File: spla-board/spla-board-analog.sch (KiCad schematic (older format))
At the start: 23 parts, among them J13 J_ANALOG, J14 J_AREF, U4 AD9280ARS, U5 AD9280ARS, U6 AD9280ARS

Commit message: schematic: Partial rework of analog to use LMH6611 + ADC1173.
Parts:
- removed C16, C18, C19, C20, C22, C23, C24, C26, C27: 0.1uF, Capacitor_SMD:C_0603_1608Metric, symbol Device:C_Small
- removed C17, C21, C25: 10uF, Capacitor_SMD:C_0603_1608Metric, symbol Device:C_Small
- removed U4, U5, U6: AD9280ARS, Package_SO:SSOP-28_5.3x10.2mm_P0.65mm, symbol Analog_ADC:AD9280ARS
- added C?: 0.1uF, Capacitor_SMD:C_0603_1608Metric, symbol Device:C_Small
- added C?: 10uF, Capacitor_SMD:C_0603_1608Metric, symbol Device:C_Small
- added C? (x5): 0.1uF, symbol Device:C_Small
- added C? (x3): 10uF, symbol Device:C_Small
- added C?: 150pF, symbol Device:C_Small
- added C?: 5.6uF, symbol Device:C_Small
- added C?: 390pF, symbol Device:C_Small
- added C?: 0.01uF, symbol Device:C_Small
- added C?: 1nF, symbol Device:C_Small
- added C?: 1uF, symbol Device:C_Small
- added R?: 100,1%, Resistor_SMD:R_0603_1608Metric, symbol Device:R_Small
- added R?: 300, symbol Device:R
- added R?: 720, symbol Device:R
- added R?: 1k, symbol Device:R
- added R? (x2): 14.3k, symbol Device:R_Small
- added R?: 1.24k, symbol Device:R_Small
- added R? (x2): 549, symbol Device:R_Small
- added R?: 22, symbol Device:R_Small
- added U4, U5, U6: ADC1173, symbol Analog_ADC:ADC1173
- added U?: LMH6611, Package_TO_SOT_SMD:TSOT-23-6, symbol Amplifier_Operational:LMH6611
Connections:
- net labels added: ANALOG_AMP_R, ANALOG_SCALED_R, AREF_HI, AREF_LO, OPAMP_2V5
- net labels removed: ANALOG_B_OTR, ANALOG_G_OTR, ANALOG_REF_HI, ANALOG_REF_LO, ANALOG_R_OTR
- wire segments 132 -> 144
- no-connect marks 6 -> 2
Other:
- note added: "AREF_HI = 3.1V"
- note added: "AREF_LO = 1.1V"
- note added: "Ref: ADC1173 Datasheet page 19"
- note added: "Ref: LMH6611 Datasheet Page 25"
- note added: "Ref: Nothing; bogus level divider nonsense"
- note added: "TODO: Correct these values."
- note added: "TODO: Inject opamps to maintain levels"
- note added: "TODO: Recalculate these resistors"
- note added: "TODO: Validate all this nonense with somebody who knows what they're doing."
- note added: "Vrange = 0v - 2.7v"
- note added: "Vrange = 1.2v - 3.0v"
- note removed: "2.702V Reference"
- note removed: "Clamp: Disabled"
- note removed: "Mode: External Reference"
- note removed: "No Standby"
- note removed: "No Tristate"
- note removed: "TODO: Make this voltage reference more easily tweakable."
- moved on the sheet: C14, C15, R15, R16

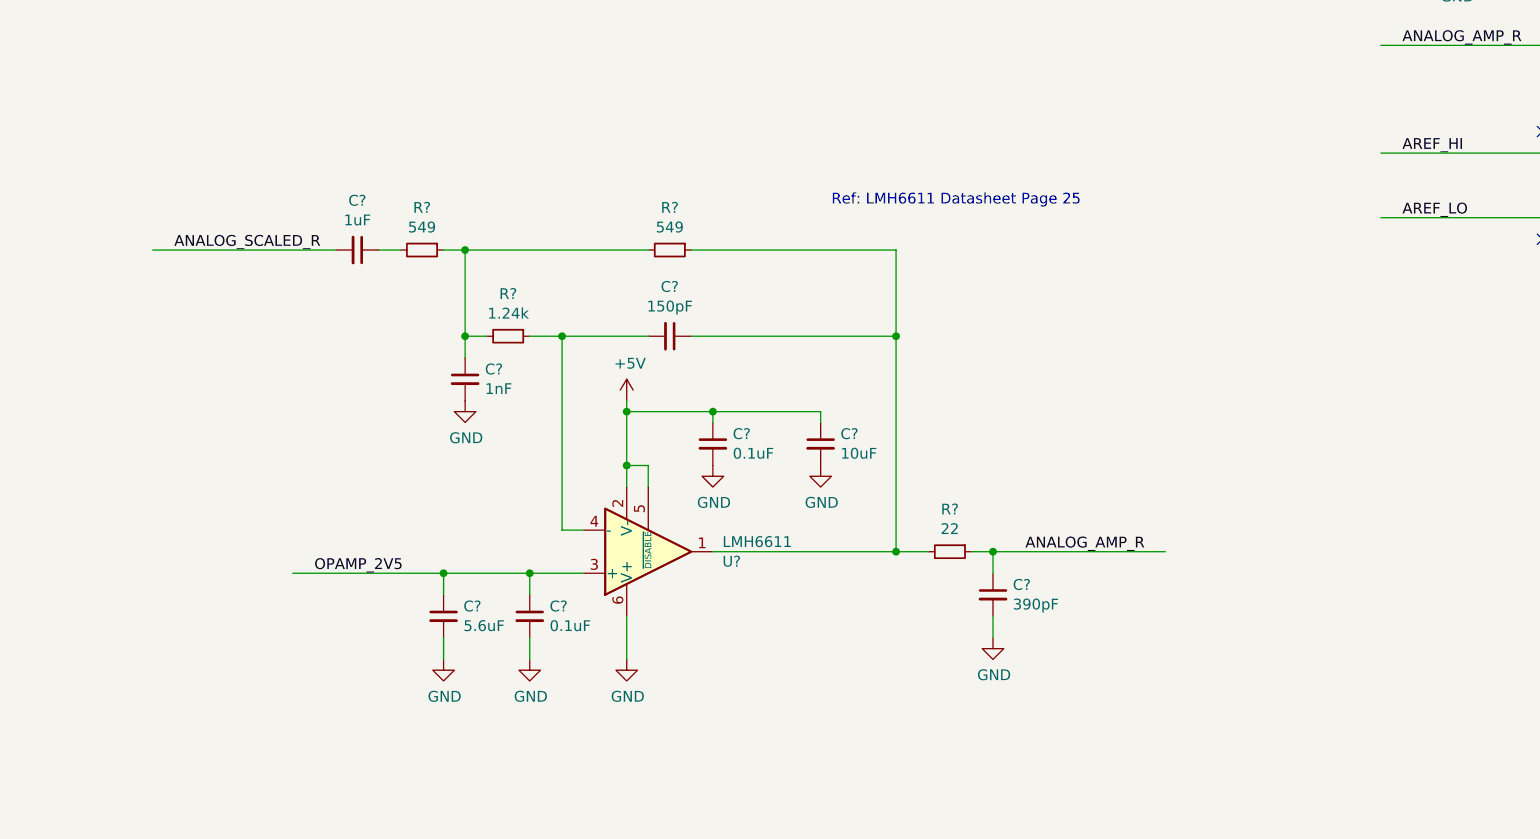
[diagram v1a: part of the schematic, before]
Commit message: schematic: More fiddling with analog.
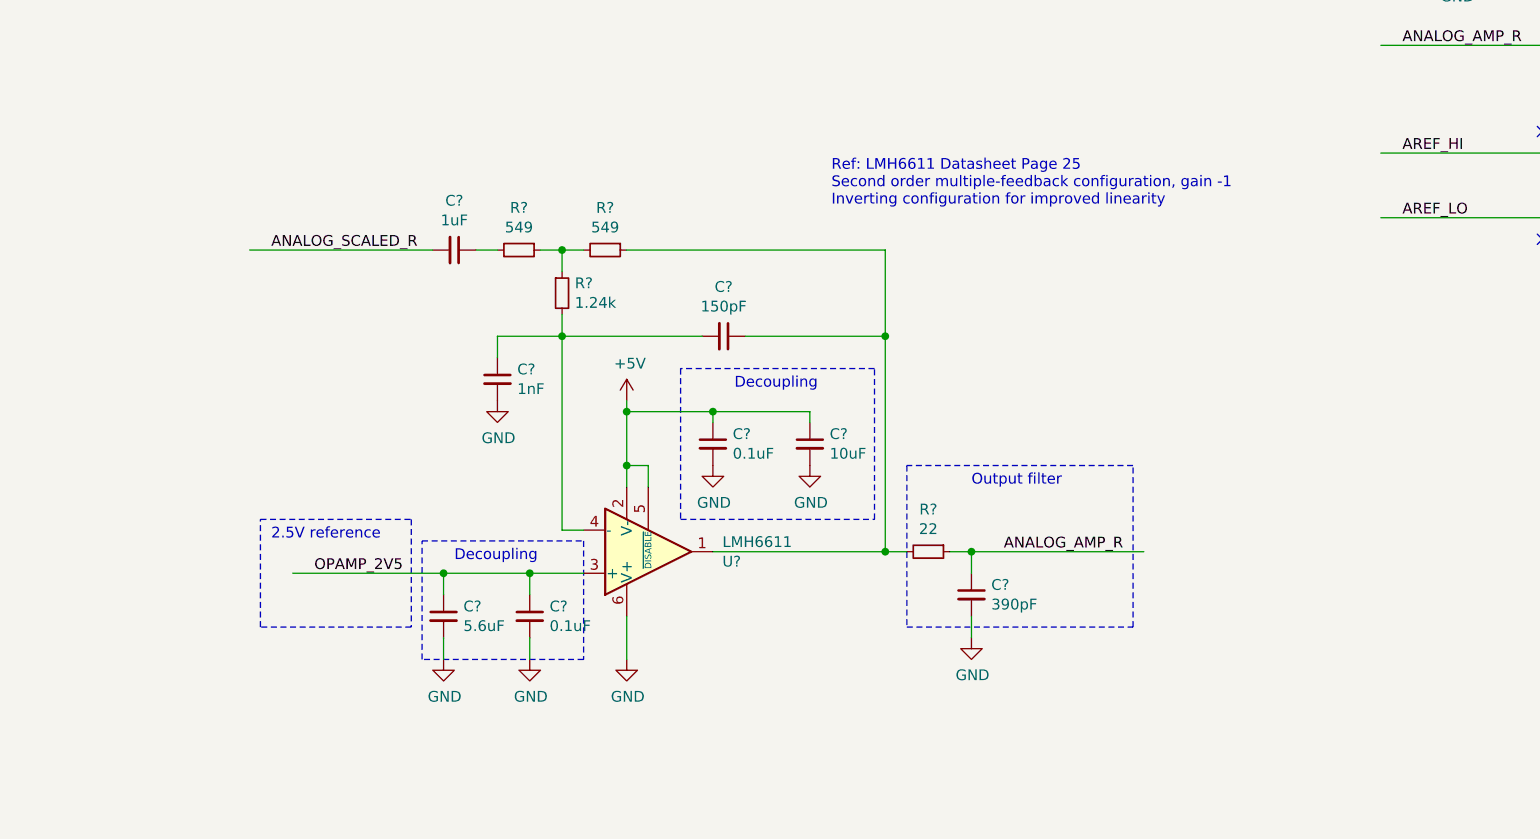
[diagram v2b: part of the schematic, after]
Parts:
- removed R?: 1.24k, symbol Device:R_Small
- added R?: 1.24k, symbol Device:R_Small
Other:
- note added: "2.5V reference"
- note added: "Decoupling"
- note added: "Output filter"
- note added: "Ref: LMH6611 Datasheet Page 25\nSecond order multiple-feedback configuration, gain -1\nInverting configuration for improved linearity"
- note removed: "Ref: LMH6611 Datasheet Page 25"
- moved on the sheet: C?, R?

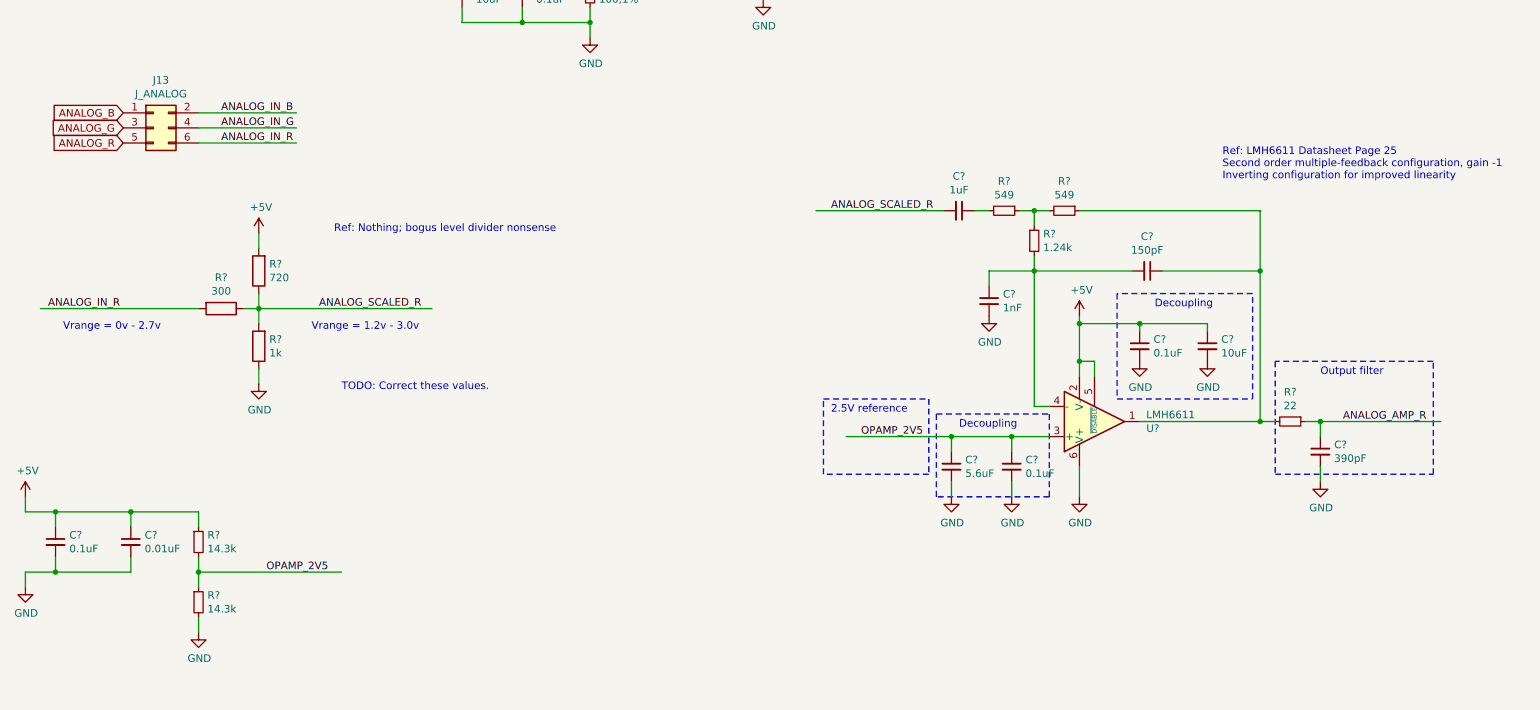
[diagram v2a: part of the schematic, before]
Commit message: schematic: More opamp fiddling.
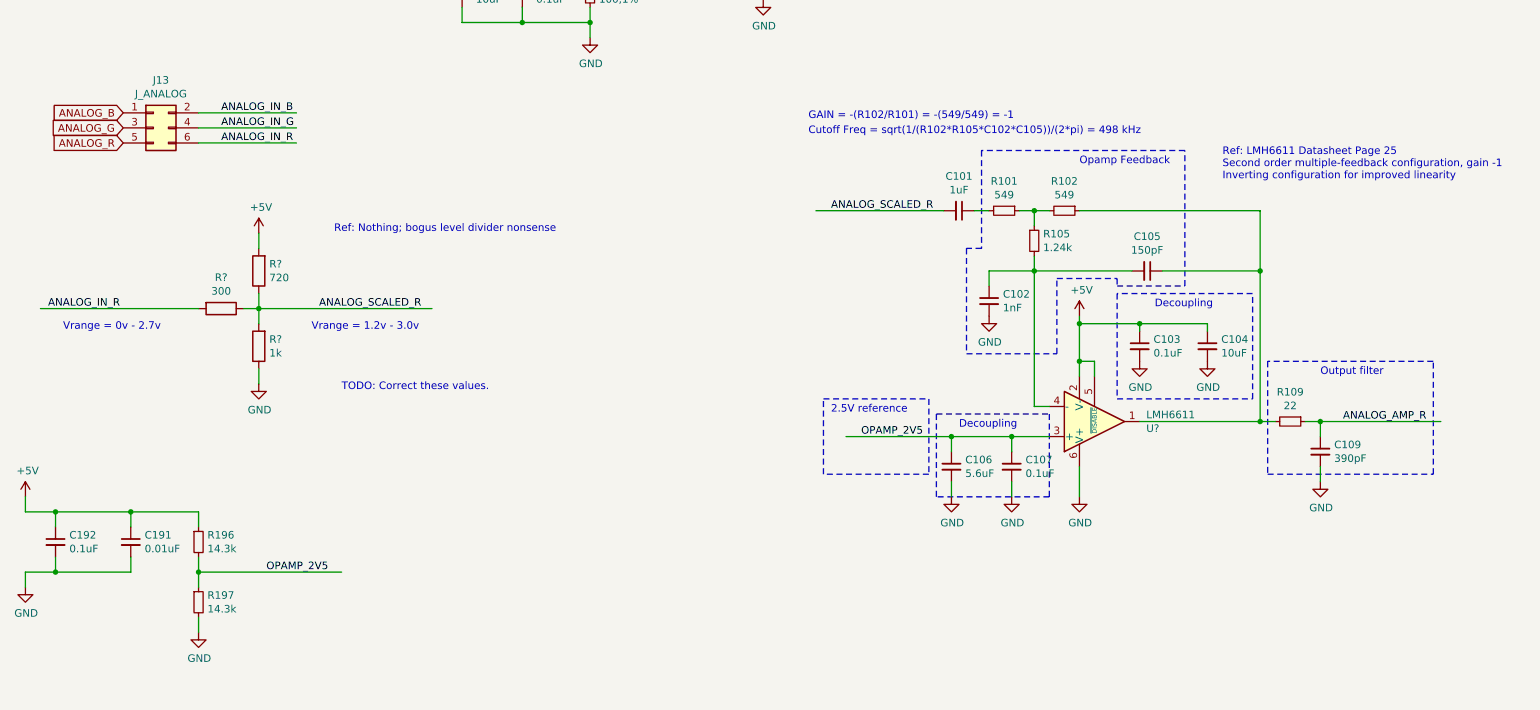
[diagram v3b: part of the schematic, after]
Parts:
- gave numbers to parts that had none: 16
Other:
- note added: "Cutoff Freq = sqrt(1/(R102*R105*C102*C105))/(2*pi) = 498 kHz"
- note added: "GAIN = -(R102/R101) = -(549/549) = -1"
- note added: "Opamp Feedback"
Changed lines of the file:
@@
 	13350 4100 13550 4100
 $Comp
-L power:GND #PWR?
+L power:GND #PWR0196
 U 1 1 5E99F9E8
 P 13550 4200
-F 0 "#PWR?" H 13550 3950 50  0001 C CNN
+F 0 "#PWR0196" H 13550 3950 50  0001 C CNN
 F 1 "GND" H 13555 4027 50  0000 C CNN
 F 2 "" H 13550 4200 50  0001 C CNN
@@
 	12950 4100 12700 4100
 $Comp
-L power:GND #PWR?
+L power:GND #PWR0207
 U 1 1 5E9A0D5B
 P 12700 4200
-F 0 "#PWR?" H 12700 3950 50  0001 C CNN
+F 0 "#PWR0207" H 12700 3950 50  0001 C CNN
 F 1 "GND" H 12705 4027 50  0000 C CNN
 F 2 "" H 12700 4200 50  0001 C CNN
@@
 	13350 2400 13350 2500
 $Comp
-L power:+3V3 #PWR?
+L power:+3V3 #PWR0208
 U 1 1 5E9A44F8
 P 13350 1850
-F 0 "#PWR?" H 13350 1700 50  0001 C CNN
+F 0 "#PWR0208" H 13350 1700 50  0001 C CNN
 F 1 "+3V3" H 13365 2023 50  0000 C CNN
 F 2 "" H 13350 1850 50  0001 C CNN
@@
 	12950 2400 12850 2400
 $Comp
-L power:+5V #PWR?
+L power:+5V #PWR0209
 U 1 1 5E9A757C
 P 12850 1850
-F 0 "#PWR?" H 12850 1700 50  0001 C CNN
+F 0 "#PWR0209" H 12850 1700 50  0001 C CNN
 F 1 "+5V" H 12865 2023 50  0000 C CNN
 F 2 "" H 12850 1850 50  0001 C CNN
@@
 $EndComp
 $Comp
-L power:GND #PWR?
+L power:GND #PWR0210
 U 1 1 5E9A7B1B
 P 8200 5750
-F 0 "#PWR?" H 8200 5500 50  0001 C CNN
+F 0 "#PWR0210" H 8200 5500 50  0001 C CNN
 F 1 "GND" H 8205 5577 50  0000 C CNN
 F 2 "" H 8200 5750 50  0001 C CNN
@@
 $EndComp
 $Comp
-L Device:C_Small C?
+L Device:C_Small C105
 U 1 1 5E9ACDDD
 P 8650 4250
-F 0 "C?" V 8421 4250 50  0000 C CNN
+F 0 "C105" V 8421 4250 50  0000 C CNN
 F 1 "150pF" V 8512 4250 50  0000 C CNN
 F 2 "" H 8650 4250 50  0001 C CNN
@@
 $EndComp
 $Comp
-L Device:C_Small C?
+L Device:C_Small C106
 U 1 1 5E9AE271
 P 7350 5550
-F 0 "C?" H 7442 5596 50  0000 L CNN
+F 0 "C106" H 7442 5596 50  0000 L CNN
 F 1 "5.6uF" H 7442 5505 50  0000 L CNN
 F 2 "" H 7350 5550 50  0001 C CNN
@@
 $EndComp
 $Comp
-L Device:C_Small C?
+L Device:C_Small C107
 U 1 1 5E9AE27B
 P 7750 5550
-F 0 "C?" H 7842 5596 50  0000 L CNN
+F 0 "C107" H 7842 5596 50  0000 L CNN
 F 1 "0.1uF" H 7842 5505 50  0000 L CNN
 F 2 "" H 7750 5550 50  0001 C CNN
@@
 $EndComp
 $Comp
-L Device:C_Small C?
+L Device:C_Small C109
 U 1 1 5E9AFAB1
 P 9800 5450
-F 0 "C?" H 9892 5496 50  0000 L CNN
+F 0 "C109" H 9892 5496 50  0000 L CNN
 F 1 "390pF" H 9892 5405 50  0000 L CNN
 F 2 "" H 9800 5450 50  0001 C CNN
@@
 $EndComp
 $Comp
-L Device:C_Small C?
+L Device:C_Small C192
 U 1 1 5E9B0FA6
 P 1400 6050
-F 0 "C?" H 1492 6096 50  0000 L CNN
+F 0 "C192" H 1492 6096 50  0000 L CNN
 F 1 "0.1uF" H 1492 6005 50  0000 L CNN
 F 2 "" H 1400 6050 50  0001 C CNN
@@
 $EndComp
 $Comp
-L Device:C_Small C?
+L Device:C_Small C191
 U 1 1 5E9B0FB0
 P 1900 6050
-F 0 "C?" H 1992 6096 50  0000 L CNN
+F 0 "C191" H 1992 6096 50  0000 L CNN
 F 1 "0.01uF" H 1992 6005 50  0000 L CNN
 F 2 "" H 1900 6050 50  0001 C CNN
@@
 $EndComp
 $Comp
-L Device:R_Small R?
+L Device:R_Small R197
 U 1 1 5E9B33F1
 P 2350 6450
-F 0 "R?" H 2409 6496 50  0000 L CNN
+F 0 "R197" H 2409 6496 50  0000 L CNN
 F 1 "14.3k" H 2409 6405 50  0000 L CNN
 F 2 "" H 2350 6450 50  0001 C CNN
@@
 $EndComp
 $Comp
-L Device:R_Small R?
+L Device:R_Small R196
 U 1 1 5E9B4953
 P 2350 6050
-F 0 "R?" H 2409 6096 50  0000 L CNN
+F 0 "R196" H 2409 6096 50  0000 L CNN
 F 1 "14.3k" H 2409 6005 50  0000 L CNN
 F 2 "" H 2350 6050 50  0001 C CNN
@@
 $EndComp
 $Comp
-L Device:C_Small C?
+L Device:C_Small C102
 U 1 1 5E9B7525
 P 7600 4450
-F 0 "C?" H 7692 4496 50  0000 L CNN
+F 0 "C102" H 7692 4496 50  0000 L CNN
 F 1 "1nF" H 7692 4405 50  0000 L CNN
 F 2 "" H 7600 4450 50  0001 C CNN
@@
 $EndComp
 $Comp
-L Device:R_Small R?
+L Device:R_Small R102
 U 1 1 5E9B8A3B
 P 8100 3850
-F 0 "R?" V 7904 3850 50  0000 C CNN
+F 0 "R102" V 7904 3850 50  0000 C CNN
 F 1 "549" V 7995 3850 50  0000 C CNN
 F 2 "" H 8100 3850 50  0001 C CNN
@@
 $EndComp
 $Comp
-L Device:R_Small R?
+L Device:R_Small R101
 U 1 1 5E9B9EA4
 P 7700 3850
-F 0 "R?" V 7504 3850 50  0000 C CNN
+F 0 "R101" V 7504 3850 50  0000 C CNN
 F 1 "549" V 7595 3850 50  0000 C CNN
 F 2 "" H 7700 3850 50  0001 C CNN
@@
 $EndComp
 $Comp
-L Device:C_Small C?
+L Device:C_Small C101
 U 1 1 5E9BBA79
 P 7400 3850
-F 0 "C?" V 7171 3850 50  0000 C CNN
+F 0 "C101" V 7171 3850 50  0000 C CNN
 F 1 "1uF" V 7262 3850 50  0000 C CNN
 F 2 "" H 7400 3850 50  0001 C CNN
@@
 	7600 4250 7600 4350
 $Comp
-L power:GND #PWR?
+L power:GND #PWR0211
 U 1 1 5E9D05AB
 P 7600 4550
-F 0 "#PWR?" H 7600 4300 50  0001 C CNN
+F 0 "#PWR0211" H 7600 4300 50  0001 C CNN
 F 1 "GND" H 7605 4377 50  0000 C CNN
 F 2 "" H 7600 4550 50  0001 C CNN
@@
 	1400 5850 1900 5850
 $Comp
-L power:+5V #PWR?
+L power:+5V #PWR0212
 U 1 1 5E9D8602
 P 2750 4000
-F 0 "#PWR?" H 2750 3850 50  0001 C CNN
+F 0 "#PWR0212" H 2750 3850 50  0001 C CNN
 F 1 "+5V" H 2765 4173 50  0000 C CNN
 F 2 "" H 2750 4000 50  0001 C CNN
@@
 	2750 4100 2750 4000
 $Comp
-L power:GND #PWR?
+L power:GND #PWR0213
 U 1 1 5E9DA76B
 P 2750 5000
-F 0 "#PWR?" H 2750 4750 50  0001 C CNN
+F 0 "#PWR0213" H 2750 4750 50  0001 C CNN
 F 1 "GND" H 2755 4827 50  0000 C CNN
 F 2 "" H 2750 5000 50  0001 C CNN
@@
 	2750 4900 2750 5000
 $Comp
-L power:+5V #PWR?
+L power:+5V #PWR0214
 U 1 1 5E9DC9C9
 P 1200 5750
-F 0 "#PWR?" H 1200 5600 50  0001 C CNN
+F 0 "#PWR0214" H 1200 5600 50  0001 C CNN
 F 1 "+5V" H 1215 5923 50  0000 C CNN
 F 2 "" H 1200 5750 50  0001 C CNN
@@
 $EndComp
 $Comp
-L power:GND #PWR?
+L power:GND #PWR0215
 U 1 1 5E9DEC96
 P 1200 6350
-F 0 "#PWR?" H 1200 6100 50  0001 C CNN
+F 0 "#PWR0215" H 1200 6100 50  0001 C CNN
 F 1 "GND" H 1205 6177 50  0000 C CNN
 F 2 "" H 1200 6350 50  0001 C CNN
@@
 	2350 6550 2350 6650
 $Comp
-L power:GND #PWR?
+L power:GND #PWR0216
 U 1 1 5E9EAF0C
 P 2350 6650
-F 0 "#PWR?" H 2350 6400 50  0001 C CNN
+F 0 "#PWR0216" H 2350 6400 50  0001 C CNN
 F 1 "GND" H 2355 6477 50  0000 C CNN
 F 2 "" H 2350 6650 50  0001 C CNN
@@
 $EndComp
 $Comp
-L power:GND #PWR?
+L power:GND #PWR0217
 U 1 1 5E9F0655
 P 7350 5750
-F 0 "#PWR?" H 7350 5500 50  0001 C CNN
+F 0 "#PWR0217" H 7350 5500 50  0001 C CNN
 F 1 "GND" H 7355 5577 50  0000 C CNN
 F 2 "" H 7350 5750 50  0001 C CNN
@@
 	2350 6250 3300 6250
 $Comp
-L power:GND #PWR?
+L power:GND #PWR0218
 U 1 1 5E9F2D31
 P 7750 5750
-F 0 "#PWR?" H 7750 5500 50  0001 C CNN
+F 0 "#PWR0218" H 7750 5500 50  0001 C CNN
 F 1 "GND" H 7755 5577 50  0000 C CNN
 F 2 "" H 7750 5750 50  0001 C CNN
@@
 	1200 5850 1200 5750
 $Comp
-L Device:R_Small R?
+L Device:R_Small R109
 U 1 1 5EA04950
 P 9600 5250
-F 0 "R?" V 9404 5250 50  0000 C CNN
+F 0 "R109" V 9404 5250 50  0000 C CNN
 F 1 "22" V 9495 5250 50  0000 C CNN
 F 2 "" H 9600 5250 50  0001 C CNN
@@
 $EndComp
 $Comp
-L power:GND #PWR?
+L power:GND #PWR0219
 U 1 1 5EA05495
 P 9800 5650
-F 0 "#PWR?" H 9800 5400 50  0001 C CNN
+F 0 "#PWR0219" H 9800 5400 50  0001 C CNN
 F 1 "GND" H 9805 5477 50  0000 C CNN
 F 2 "" H 9800 5650 50  0001 C CNN
@@
 $EndComp
 $Comp
-L power:GND #PWR?
+L power:GND #PWR0220
 U 1 1 5EA5AFB3
 P 12050 2500
-F 0 "#PWR?" H 12050 2250 50  0001 C CNN
+F 0 "#PWR0220" H 12050 2250 50  0001 C CNN
 F 1 "GND" H 12055 2327 50  0000 C CNN
 F 2 "" H 12050 2500 50  0001 C CNN
@@
 	13350 2000 13350 2400
 $Comp
-L power:GND #PWR?
+L power:GND #PWR0221
 U 1 1 5EA905F2
 P 14000 2500
-F 0 "#PWR?" H 14000 2250 50  0001 C CNN
+F 0 "#PWR0221" H 14000 2250 50  0001 C CNN
 F 1 "GND" H 14005 2327 50  0000 C CNN
 F 2 "" H 14000 2500 50  0001 C CNN
@@
 	8200 5550 8200 5750
 $Comp
-L power:+5V #PWR?
+L power:+5V #PWR0222
 U 1 1 5EAB0252
 P 8200 4550
-F 0 "#PWR?" H 8200 4400 50  0001 C CNN
+F 0 "#PWR0222" H 8200 4400 50  0001 C CNN
 F 1 "+5V" H 8215 4723 50  0000 C CNN
 F 2 "" H 8200 4550 50  0001 C CNN
@@
 Connection ~ 8200 4600
 $Comp
-L power:GND #PWR?
+L power:GND #PWR0223
 U 1 1 5E9C5E2E
 P 9050 4850
-F 0 "#PWR?" H 9050 4600 50  0001 C CNN
+F 0 "#PWR0223" H 9050 4600 50  0001 C CNN
 F 1 "GND" H 9055 4677 50  0000 C CNN
 F 2 "" H 9050 4850 50  0001 C CNN
@@
 $EndComp
 $Comp
-L power:GND #PWR?
+L power:GND #PWR0224
 U 1 1 5E9C48E2
 P 8600 4850
-F 0 "#PWR?" H 8600 4600 50  0001 C CNN
+F 0 "#PWR0224" H 8600 4600 50  0001 C CNN
 F 1 "GND" H 8605 4677 50  0000 C CNN
 F 2 "" H 8600 4850 50  0001 C CNN
@@
 $EndComp
 $Comp
-L Device:C_Small C?
+L Device:C_Small C104
 U 1 1 5E9AB6FD
 P 9050 4750
-F 0 "C?" H 9142 4796 50  0000 L CNN
+F 0 "C104" H 9142 4796 50  0000 L CNN
 F 1 "10uF" H 9142 4705 50  0000 L CNN
 F 2 "" H 9050 4750 50  0001 C CNN
@@
 $EndComp
 $Comp
-L Device:C_Small C?
+L Device:C_Small C103
 U 1 1 5E9AB3D5
 P 8600 4750
-F 0 "C?" H 8692 4796 50  0000 L CNN
+F 0 "C103" H 8692 4796 50  0000 L CNN
 F 1 "0.1uF" H 8692 4705 50  0000 L CNN
 F 2 "" H 8600 4750 50  0001 C CNN
@@
 	8200 4850 8200 4950
 $Comp
-L Device:R_Small R?
+L Device:R_Small R105
 U 1 1 5E9577DD
 P 7900 4050
-F 0 "R?" H 7959 4096 50  0000 L CNN
+F 0 "R105" H 7959 4096 50  0000 L CNN
 F 1 "1.24k" H 7959 4005 50  0000 L CNN
 F 2 "" H 7900 4050 50  0001 C CNN
@@
 	6500 5600 6500 5100
 Wire Notes Line
-	9500 4850 9500 5600
-Wire Notes Line
-	9500 5600 10550 5600
+	9450 4850 9450 5600
+Wire Notes Line
+	9450 5600 10550 5600
 Wire Notes Line
 	10550 5600 10550 4850
 Wire Notes Line
-	10550 4850 9500 4850
+	10550 4850 9450 4850
 Text Notes 9800 4950 0    50   ~ 0
 Output filter
@@
 Text Notes 6550 5200 0    50   ~ 0
 2.5V reference
+Text Notes 6400 3250 0    50   ~ 0
+GAIN = -(R102/R101) = -(549/549) = -1
+Text Notes 6400 3350 0    50   ~ 0
+Cutoff Freq = sqrt(1/(R102*R105*C102*C105))/(2*pi) = 498 kHz
+Wire Notes Line
+	7550 3450 7550 4100
+Wire Notes Line
+	7550 4100 7450 4100
+Wire Notes Line
+	7450 4100 7450 4800
+Wire Notes Line
+	7450 4800 8050 4800
+Wire Notes Line
+	8050 4800 8050 4300
+Wire Notes Line
+	8050 4300 8450 4300
+Wire Notes Line
+	8450 4300 8450 4350
+Wire Notes Line
+	8450 4350 8900 4350
+Wire Notes Line
+	8900 4350 8900 3450
+Wire Notes Line
+	8900 3450 7550 3450
+Text Notes 8200 3550 0    50   ~ 0
+Opamp Feedback
 $EndSCHEMATC
